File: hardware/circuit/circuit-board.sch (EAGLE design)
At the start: 14 parts, among them U1 ADUM1200CRZ

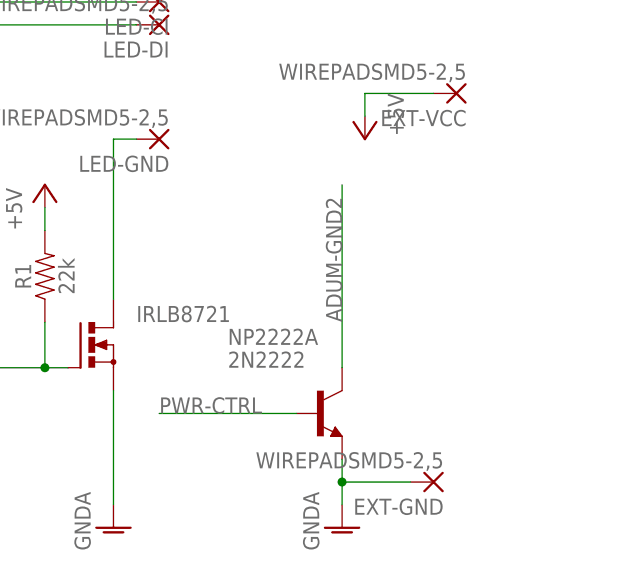
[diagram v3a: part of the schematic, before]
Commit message: Added missing 100k resistor to base of PN2222A, deleted flawed Gerber files - board layout is not updated for now because I have V2 in mind and PCBs in hand already
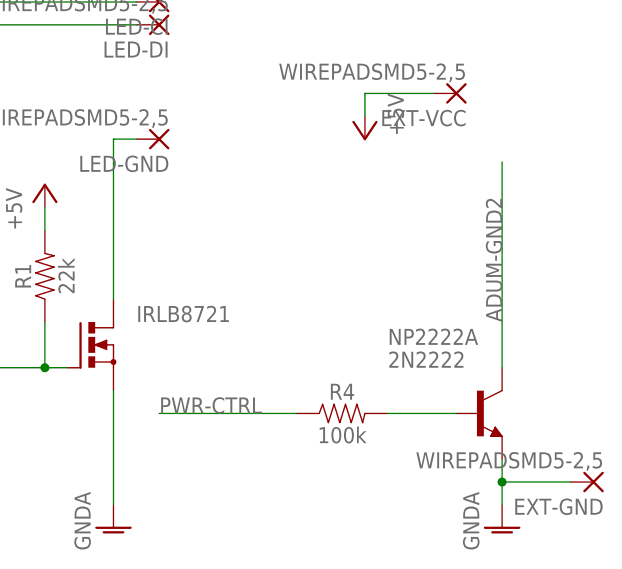
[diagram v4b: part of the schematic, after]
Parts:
- added R4: 100k, SparkFun-Resistors:100KOHM-0603-1/10W-1%
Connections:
- new net N$2: NP2222A.B, R4.2
- net PWR-CTRL: now also R4.1; no longer NP2222A.B
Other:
- moved on the sheet: EXT-GND, NP2222A
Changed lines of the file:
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@@
 <grid distance="0.1" unitdist="inch" unit="inch" style="lines" multiple="1" display="no" altdistance="0.01" altunitdist="inch" altunit="inch"/>
 <layers>
-<layer number="1" name="Top" color="4" fill="1" visible="yes" active="no"/>
-<layer number="16" name="Bottom" color="1" fill="1" visible="yes" active="no"/>
-<layer number="17" name="Pads" color="2" fill="1" visible="yes" active="no"/>
-<layer number="18" name="Vias" color="2" fill="1" visible="yes" active="no"/>
-<layer number="19" name="Unrouted" color="6" fill="1" visible="yes" active="no"/>
-<layer number="20" name="Dimension" color="15" fill="1" visible="yes" active="no"/>
-<layer number="21" name="tPlace" color="7" fill="1" visible="yes" active="no"/>
-<layer number="22" name="bPlace" color="7" fill="1" visible="yes" active="no"/>
-<layer number="23" name="tOrigins" color="15" fill="1" visible="yes" active="no"/>
-<layer number="24" name="bOrigins" color="15" fill="1" visible="yes" active="no"/>
-<layer number="25" name="tNames" color="7" fill="1" visible="yes" active="no"/>
-<layer number="26" name="bNames" color="7" fill="1" visible="yes" active="no"/>
-<layer number="27" name="tValues" color="7" fill="1" visible="yes" active="no"/>
-<layer number="28" name="bValues" color="7" fill="1" visible="yes" active="no"/>
+<layer number="1" name="Top" color="4" fill="1" visible="no" active="no"/>
+<layer number="16" name="Bottom" color="1" fill="1" visible="no" active="no"/>
+<layer number="17" name="Pads" color="2" fill="1" visible="no" active="no"/>
+<layer number="18" name="Vias" color="2" fill="1" visible="no" active="no"/>
+<layer number="19" name="Unrouted" color="6" fill="1" visible="no" active="no"/>
+<layer number="20" name="Dimension" color="15" fill="1" visible="no" active="no"/>
+<layer number="21" name="tPlace" color="7" fill="1" visible="no" active="no"/>
+<layer number="22" name="bPlace" color="7" fill="1" visible="no" active="no"/>
+<layer number="23" name="tOrigins" color="15" fill="1" visible="no" active="no"/>
+<layer number="24" name="bOrigins" color="15" fill="1" visible="no" active="no"/>
+<layer number="25" name="tNames" color="7" fill="1" visible="no" active="no"/>
+<layer number="26" name="bNames" color="7" fill="1" visible="no" active="no"/>
+<layer number="27" name="tValues" color="7" fill="1" visible="no" active="no"/>
+<layer number="28" name="bValues" color="7" fill="1" visible="no" active="no"/>
 <layer number="29" name="tStop" color="7" fill="3" visible="no" active="no"/>
 <layer number="30" name="bStop" color="7" fill="6" visible="no" active="no"/>
@@
 <layer number="35" name="tGlue" color="7" fill="4" visible="no" active="no"/>
 <layer number="36" name="bGlue" color="7" fill="5" visible="no" active="no"/>
-<layer number="37" name="tTest" color="7" fill="1" visible="yes" active="no"/>
-<layer number="38" name="bTest" color="7" fill="1" visible="yes" active="no"/>
+<layer number="37" name="tTest" color="7" fill="1" visible="no" active="no"/>
+<layer number="38" name="bTest" color="7" fill="1" visible="no" active="no"/>
 <layer number="39" name="tKeepout" color="4" fill="11" visible="no" active="no"/>
 <layer number="40" name="bKeepout" color="1" fill="11" visible="no" active="no"/>
@@
 <layer number="44" name="Drills" color="7" fill="1" visible="no" active="no"/>
 <layer number="45" name="Holes" color="7" fill="1" visible="no" active="no"/>
-<layer number="46" name="Milling" color="3" fill="1" visible="yes" active="no"/>
-<layer number="47" name="Measures" color="7" fill="1" visible="yes" active="no"/>
-<layer number="48" name="Document" color="7" fill="1" visible="yes" active="no"/>
-<layer number="49" name="Reference" color="7" fill="1" visible="yes" active="no"/>
-<layer number="50" name="dxf" color="7" fill="1" visible="yes" active="no"/>
-<layer number="51" name="tDocu" color="7" fill="1" visible="yes" active="no"/>
-<layer number="52" name="bDocu" color="7" fill="1" visible="yes" active="no"/>
-<layer number="53" name="tGND_GNDA" color="7" fill="9" visible="yes" active="no"/>
-<layer number="54" name="bGND_GNDA" color="1" fill="9" visible="yes" active="no"/>
-<layer number="56" name="wert" color="7" fill="1" visible="yes" active="no"/>
-<layer number="57" name="tCAD" color="7" fill="1" visible="yes" active="no"/>
-<layer number="59" name="tCarbon" color="7" fill="1" visible="yes" active="no"/>
-<layer number="60" name="bCarbon" color="7" fill="1" visible="yes" active="no"/>
+<layer number="46" name="Milling" color="3" fill="1" visible="no" active="no"/>
+<layer number="47" name="Measures" color="7" fill="1" visible="no" active="no"/>
+<layer number="48" name="Document" color="7" fill="1" visible="no" active="no"/>
+<layer number="49" name="Reference" color="7" fill="1" visible="no" active="no"/>
+<layer number="50" name="dxf" color="7" fill="1" visible="no" active="no"/>
+<layer number="51" name="tDocu" color="7" fill="1" visible="no" active="no"/>
+<layer number="52" name="bDocu" color="7" fill="1" visible="no" active="no"/>
+<layer number="53" name="tGND_GNDA" color="7" fill="9" visible="no" active="no"/>
+<layer number="54" name="bGND_GNDA" color="1" fill="9" visible="no" active="no"/>
+<layer number="56" name="wert" color="7" fill="1" visible="no" active="no"/>
+<layer number="57" name="tCAD" color="7" fill="1" visible="no" active="no"/>
+<layer number="59" name="tCarbon" color="7" fill="1" visible="no" active="no"/>
+<layer number="60" name="bCarbon" color="7" fill="1" visible="no" active="no"/>
 <layer number="90" name="Modules" color="5" fill="1" visible="yes" active="yes"/>
 <layer number="91" name="Nets" color="2" fill="1" visible="yes" active="yes"/>
@@
 <part name="EXT-GND" library="wirepad" deviceset="WIREPAD" device="SMD5-2,5"/>
 <part name="LED-GND" library="wirepad" deviceset="WIREPAD" device="SMD5-2,5"/>
+<part name="R4" library="SparkFun-Resistors" deviceset="100KOHM" device="-0603-1/10W-1%" value="100k"/>
 </parts>
 <sheets>
@@
 <instance part="GND4" gate="1" x="66.04" y="38.1"/>
 <instance part="U1" gate="A" x="35.56" y="91.44"/>
-<instance part="GND5" gate="1" x="91.44" y="38.1"/>
+<instance part="GND5" gate="1" x="109.22" y="38.1"/>
 <instance part="GND6" gate="1" x="12.7" y="81.28" rot="R270"/>
 <instance part="P+3" gate="1" x="10.16" y="93.98" rot="R90"/>
@@
 <instance part="GND1" gate="1" x="17.78" y="127" rot="R180"/>
 <instance part="R3" gate="G$1" x="17.78" y="106.68" rot="R270"/>
-<instance part="NP2222A" gate="G$1" x="88.9" y="50.8"/>
+<instance part="NP2222A" gate="G$1" x="106.68" y="50.8"/>
 <instance part="EXT-VCC" gate="G$1" x="104.14" y="86.36" rot="R180"/>
 <instance part="LED-CI" gate="G$1" x="71.12" y="96.52" rot="R180"/>
 <instance part="LED-DI" gate="G$1" x="71.12" y="93.98" rot="R180"/>
-<instance part="EXT-GND" gate="G$1" x="101.6" y="43.18" rot="R180"/>
+<instance part="EXT-GND" gate="G$1" x="119.38" y="43.18" rot="R180"/>
 <instance part="LED-GND" gate="G$1" x="71.12" y="81.28" rot="R180"/>
+<instance part="R4" gate="G$1" x="91.44" y="50.8"/>
 </instances>
 <busses>
@@
 <pinref part="NP2222A" gate="G$1" pin="E"/>
 <pinref part="GND5" gate="1" pin="GNDA"/>
-<wire x1="91.44" y1="40.64" x2="91.44" y2="43.18" width="0.1524" layer="91"/>
-<wire x1="91.44" y1="43.18" x2="91.44" y2="45.72" width="0.1524" layer="91"/>
-<wire x1="99.06" y1="43.18" x2="91.44" y2="43.18" width="0.1524" layer="91"/>
-<junction x="91.44" y="43.18"/>
+<wire x1="109.22" y1="40.64" x2="109.22" y2="43.18" width="0.1524" layer="91"/>
+<wire x1="109.22" y1="43.18" x2="109.22" y2="45.72" width="0.1524" layer="91"/>
+<wire x1="116.84" y1="43.18" x2="109.22" y2="43.18" width="0.1524" layer="91"/>
+<junction x="109.22" y="43.18"/>
 <pinref part="EXT-GND" gate="G$1" pin="P"/>
 </segment>
@@
 </segment>
 <segment>
-<pinref part="NP2222A" gate="G$1" pin="B"/>
+<label x="71.12" y="50.8" size="1.778" layer="95"/>
+<pinref part="R4" gate="G$1" pin="1"/>
 <wire x1="86.36" y1="50.8" x2="71.12" y2="50.8" width="0.1524" layer="91"/>
-<label x="71.12" y="50.8" size="1.778" layer="95"/>
 </segment>
 </net>
@@
 <segment>
 <pinref part="NP2222A" gate="G$1" pin="C"/>
-<wire x1="91.44" y1="55.88" x2="91.44" y2="76.2" width="0.1524" layer="91"/>
-<label x="91.44" y="60.96" size="1.778" layer="95" rot="R90"/>
+<wire x1="109.22" y1="55.88" x2="109.22" y2="78.74" width="0.1524" layer="91"/>
+<label x="109.22" y="60.96" size="1.778" layer="95" rot="R90"/>
 </segment>
 </net>
@@
 </segment>
 </net>
+<net name="N$2" class="0">
+<segment>
+<pinref part="NP2222A" gate="G$1" pin="B"/>
+<pinref part="R4" gate="G$1" pin="2"/>
+<wire x1="96.52" y1="50.8" x2="104.14" y2="50.8" width="0.1524" layer="91"/>
+</segment>
+</net>
